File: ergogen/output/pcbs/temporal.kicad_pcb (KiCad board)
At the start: 2 copper layers, 144.2 x 91.9 mm, 55 parts

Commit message: new shape
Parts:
- added D22: , ceoloide:diode_tht_sod123, F.Cu at (164.5, 118.3)
- added S22: , ceoloide:switch_choc_v1_v2, B.Cu at (168.0, 114.8)
- moved S19 15.9 mm to (114.1, 92.4), turned to 0 degrees
- moved S20 15.9 mm to (133.8, 95.0), turned to -15 degrees
- moved MH4 15.9 mm to (104.5, 92.8), turned to 10 degrees
- moved D20 15.6 mm to (132.5, 99.8), turned to -15 degrees
- moved MH3 15.6 mm to (143.4, 98.1), turned to -15 degrees
- moved D21 15.5 mm to (149.7, 107.0), turned to -30 degrees
- moved S21 15.3 mm to (152.2, 102.6), turned to -30 degrees
- moved D19 15.2 mm to (114.1, 97.4), turned to 0 degrees
- moved RE1 14.9 mm to (94.9, 94.0), turned to 10 degrees
- moved S18 14.9 mm to (94.9, 94.0), turned to 10 degrees
- moved D18 14.1 mm to (95.8, 99.0), turned to 10 degrees
- moved D10 11.9 mm to (100.5, 51.3)
- moved D11 11.9 mm to (100.5, 34.3)
- moved D9 11.9 mm to (100.5, 68.3)
- moved S10 11.9 mm to (100.5, 46.3)
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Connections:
- RE1 pad S1: col_ring -> col_pinky
- S18 pad 2: col_ring -> col_pinky
- S19 pad 2: col_middle -> col_ring
- S20 pad 2: col_index -> col_middle
- S21 pad 2: col_inner -> col_index
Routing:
- net col_pinky: track 56.0 -> 74.7 mm, vias 3 -> 4
- net extra_thumb: track 0.00 -> 11.1 mm, vias 0 -> 2
- net row_thumb: track 9.60 -> 12.0 mm, vias 4 -> 5
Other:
- board size 144.2 x 91.9 mm -> 147.1 x 107.2 mm

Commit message: update generated files
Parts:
- moved MH3 20.0 mm to (160.6, 108.1), turned to -30 degrees
- moved MH4 19.6 mm to (124.1, 92.9), turned to 0 degrees
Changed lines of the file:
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@@
   (title_block
     (title "temporal")
-    (date "2025-11-10")
+    (date "2025-11-12")
     (rev "1")
     (company "curtis bollinger")
@@
   (footprint "ceoloide:mounting_hole_npth"
     (layer "F.Cu")
-    (at 143.3735818 98.05513279999998 -15)
+    (at 160.64669740000002 108.05669409999999 -30)
     (property "Reference" "MH3"
-      (at 0 2.55 -15)
+      (at 0 2.55 -30)
       (layer "F.SilkS")
       hide
@@
     )
     (pad "" np_thru_hole circle
-      (at 0 0 -15)
+      (at 0 0 -30)
       (size 5 5)
       (drill 5)
@@
   (footprint "ceoloide:mounting_hole_npth"
     (layer "F.Cu")
-    (at 104.4990997 92.84759689999998 10)
+    (at 124.10043890000001 92.86497739999999 0)
     (property "Reference" "MH4"
-      (at 0 2.55 10)
+      (at 0 2.55 0)
       (layer "F.SilkS")
       hide
@@
     )
     (pad "" np_thru_hole circle
-      (at 0 0 10)
+      (at 0 0 0)
       (size 5 5)
       (drill 5)

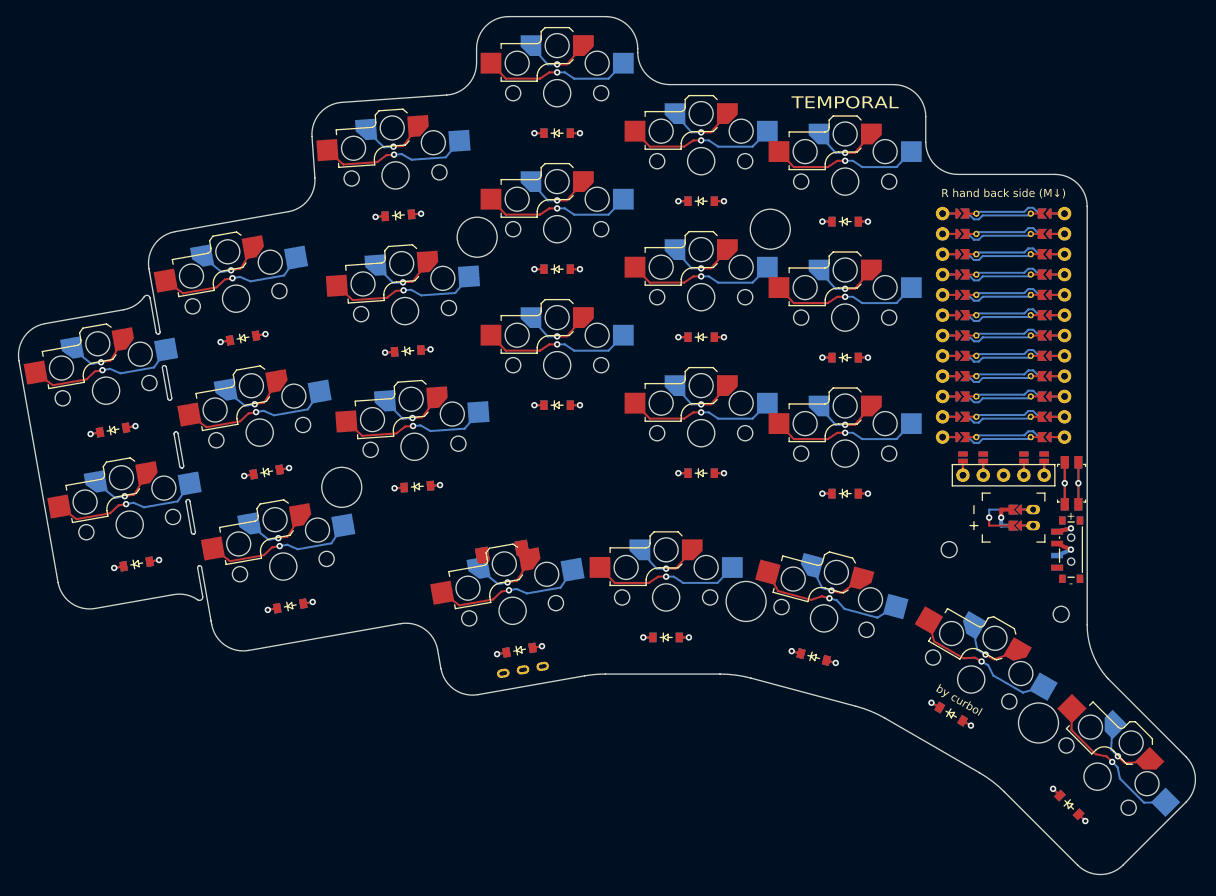
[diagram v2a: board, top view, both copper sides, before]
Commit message: working on new case
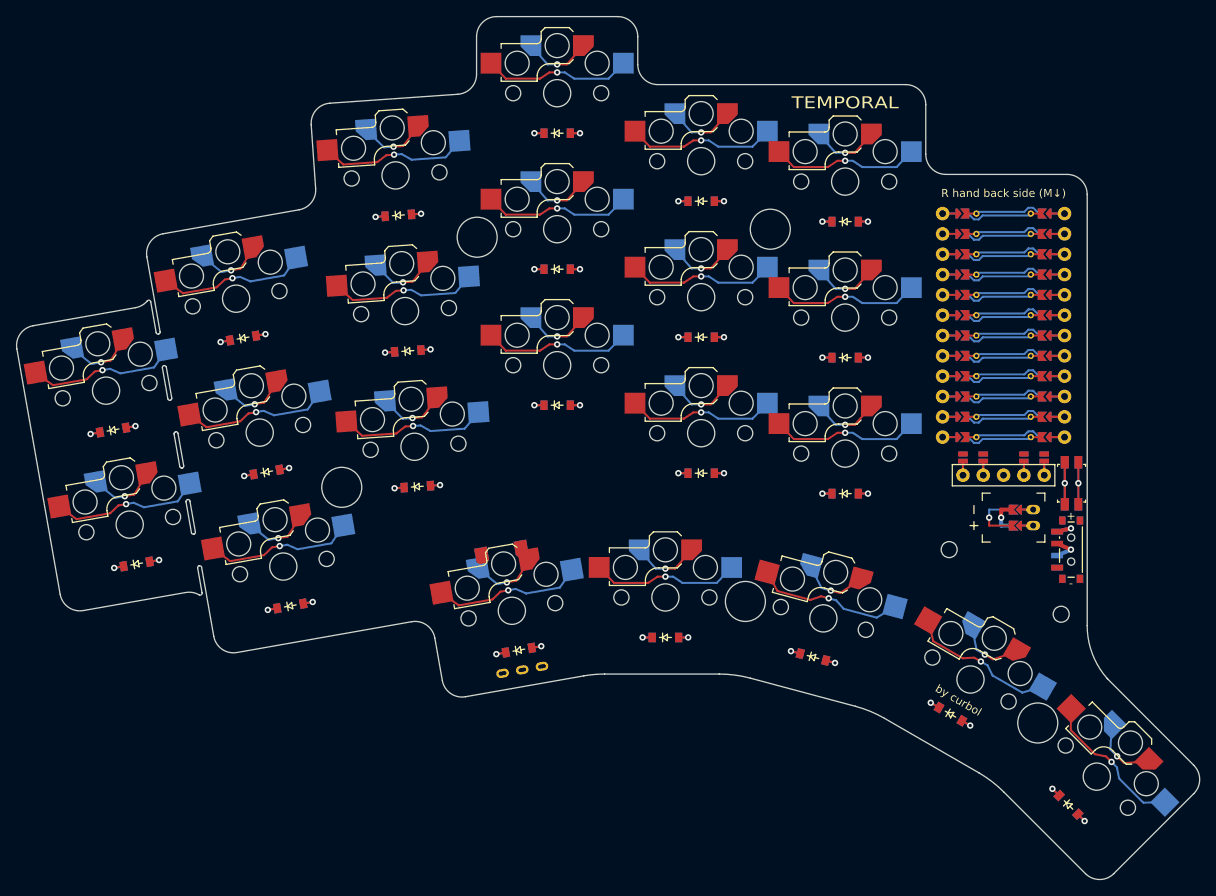
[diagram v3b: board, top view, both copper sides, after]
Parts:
- moved D18 0.09 mm to (95.7, 99.0)
- moved D19 0.09 mm to (114.0, 97.4)
- moved MH4 0.09 mm to (124.0, 92.9)
- moved RE1 0.09 mm to (94.8, 94.0)
- moved S18 0.09 mm to (94.8, 94.0)
- moved S19 0.09 mm to (114.0, 92.4)
- moved D20 0.09 mm to (132.5, 99.8)
- moved D21 0.09 mm to (149.6, 107.0)
- moved D22 0.09 mm to (164.4, 118.3)
- moved MH3 0.09 mm to (160.6, 108.1)
- moved S20 0.09 mm to (133.8, 95.0)
- moved S21 0.09 mm to (152.1, 102.6)
- moved S22 0.09 mm to (167.9, 114.8)
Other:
- board size 147.1 x 107.2 mm -> 147.9 x 107.9 mm

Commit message: folder cleanup
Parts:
- moved MH3 20.0 mm to (143.3, 98.1), turned to -15 degrees
- moved MH4 19.7 mm to (104.4, 92.9), turned to 10 degrees
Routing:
- net (no net): track 337.7 -> 0.00 mm
- net GND: track 17.9 -> 47.4 mm
- net row_thumb: track 12.0 -> 21.8 mm
- net MOSI: track 0.00 -> 9.84 mm
- net encoder_b: track 0.00 -> 9.84 mm
- net encoder_a: track 0.00 -> 9.84 mm
- net P3: track 0.00 -> 9.84 mm
- net P2: track 0.00 -> 9.84 mm
- net SCK: track 0.00 -> 9.84 mm
- net row_bottom: track 12.0 -> 21.8 mm
- net row_top: track 14.4 -> 24.2 mm
- net row_home: track 14.4 -> 24.2 mm
- net col_ring: track 74.7 -> 84.5 mm
- net col_pinky: track 74.7 -> 84.5 mm
- net col_extra: track 37.3 -> 47.2 mm
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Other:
- outline, holes or cut-outs redrawn
